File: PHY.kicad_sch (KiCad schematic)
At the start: 52 parts, among them U1 LAN83C185-JT, Y1 25 MHz

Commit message: did a lot more routing, phy nearly done
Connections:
- net MAG-RXn renamed MAG-RXN
- net MAG-RXp renamed MAG-RXP
- net MAG-TXn renamed MAG-TXN
- net MAG-TXp renamed MAG-TXP
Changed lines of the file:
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@@
     )
   )
-  (global_label "MAG-TXp" (shape input) (at 190.5 82.55 0) (fields_autoplaced)
+  (global_label "MAG-TXP" (shape input) (at 190.5 82.55 0) (fields_autoplaced)
     (effects (font (size 1.27 1.27)) (justify left))
-    (property "Intersheet References" "${INTERSHEET_REFS}" (id 0) (at 201.6217 82.6294 0)
+    (property "Intersheet References" "${INTERSHEET_REFS}" (id 0) (at 201.7426 82.4706 0)
       (effects (font (size 1.27 1.27)) (justify left) hide)
     )
@@
     )
   )
-  (global_label "MAG-TXn" (shape input) (at 190.5 85.09 0) (fields_autoplaced)
+  (global_label "MAG-TXN" (shape input) (at 190.5 85.09 0) (fields_autoplaced)
     (effects (font (size 1.27 1.27)) (justify left))
-    (property "Intersheet References" "${INTERSHEET_REFS}" (id 0) (at 201.6217 85.0106 0)
+    (property "Intersheet References" "${INTERSHEET_REFS}" (id 0) (at 201.8031 85.0106 0)
       (effects (font (size 1.27 1.27)) (justify left) hide)
     )
@@
     )
   )
-  (global_label "MAG-RXn" (shape input) (at 190.5 74.93 0) (fields_autoplaced)
+  (global_label "MAG-RXN" (shape input) (at 190.5 74.93 0) (fields_autoplaced)
     (effects (font (size 1.27 1.27)) (justify left))
-    (property "Intersheet References" "${INTERSHEET_REFS}" (id 0) (at 201.9241 74.8506 0)
+    (property "Intersheet References" "${INTERSHEET_REFS}" (id 0) (at 202.1055 74.8506 0)
       (effects (font (size 1.27 1.27)) (justify left) hide)
     )
@@
     )
   )
-  (global_label "MAG-RXp" (shape input) (at 190.5 72.39 0) (fields_autoplaced)
+  (global_label "MAG-RXP" (shape input) (at 190.5 72.39 0) (fields_autoplaced)
     (effects (font (size 1.27 1.27)) (justify left))
-    (property "Intersheet References" "${INTERSHEET_REFS}" (id 0) (at 201.9241 72.3106 0)
+    (property "Intersheet References" "${INTERSHEET_REFS}" (id 0) (at 202.045 72.3106 0)
       (effects (font (size 1.27 1.27)) (justify left) hide)
     )

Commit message: Update sourcing URLs
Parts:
- D1, D5: Source https://onecall.farnell.com/dialight/599-0240-007f/led-yellow-126mcd-590nm-1206/dp/3548450?st=yellow -> https://onecall.farnell.com/dialight/599-0240-007f/led-yellow-126mcd-590nm-1206/dp/3548450
- FB1, FB2, FB3: Source https://uk.farnell.com/bourns/mh3261-601y/ferrite-bead-0-1o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 -> https://onecall.farnell.com/bourns/mh3261-601y/ferrite-bead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
- U1: Source https://uk.rs-online.com/web/p/physical-layer-transceivers/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 -> https://onecall.farnell.com/microchip/lan83c185-jt/transcei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
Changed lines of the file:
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@@
       (effects (font (size 1.27 1.27)) hide)
     )
-    (property "Source" "https://uk.farnell.com/bourns/mh3261-601y/ferrite-bead-0-1ohm-2a-1206/dp/27870" (id 4) (at 115.57 172.72 0)
+    (property "Source" "https://onecall.farnell.com/bourns/mh3261-601y/ferrite-bead-0-1ohm-2a-1206/dp/2787025" (id 4) (at 115.57 172.72 0)
       (effects (font (size 1.27 1.27)) hide)
     )
@@
       (effects (font (size 1.27 1.27)) hide)
     )
-    (property "Source" "https://onecall.farnell.com/dialight/599-0240-007f/led-yellow-126mcd-590nm-1206/dp/3548450?st=yellow" (id 4) (at 255.27 31.75 0)
+    (property "Source" "https://onecall.farnell.com/dialight/599-0240-007f/led-yellow-126mcd-590nm-1206/dp/3548450" (id 4) (at 255.27 31.75 0)
       (effects (font (size 1.27 1.27)) hide)
     )
@@
       (effects (font (size 1.27 1.27)) hide)
     )
-    (property "Source" "https://uk.farnell.com/bourns/mh3261-601y/ferrite-bead-0-1ohm-2a-1206/dp/27870" (id 4) (at 27.94 172.72 0)
+    (property "Source" "https://onecall.farnell.com/bourns/mh3261-601y/ferrite-bead-0-1ohm-2a-1206/dp/2787025" (id 4) (at 27.94 172.72 0)
       (effects (font (size 1.27 1.27)) hide)
     )
@@
       (effects (font (size 1.27 1.27)) hide)
     )
-    (property "Source" "https://uk.farnell.com/bourns/mh3261-601y/ferrite-bead-0-1ohm-2a-1206/dp/27870" (id 4) (at 80.01 172.72 0)
+    (property "Source" "https://onecall.farnell.com/bourns/mh3261-601y/ferrite-bead-0-1ohm-2a-1206/dp/2787025" (id 4) (at 80.01 172.72 0)
       (effects (font (size 1.27 1.27)) hide)
     )
@@
       (effects (font (size 1.524 1.524)) hide)
     )
-    (property "Source" "https://uk.rs-online.com/web/p/physical-layer-transceivers/6726806" (id 4) (at 93.98 49.53 0)
+    (property "Source" "https://onecall.farnell.com/microchip/lan83c185-jt/transceiver-phy-10-100-64tqfp/dp/1711344" (id 4) (at 93.98 49.53 0)
       (effects (font (size 1.27 1.27)) hide)
     )
@@
       (effects (font (size 1.27 1.27)) hide)
     )
-    (property "Source" "https://onecall.farnell.com/dialight/599-0240-007f/led-yellow-126mcd-590nm-1206/dp/3548450?st=yellow" (id 4) (at 219.71 31.75 0)
-      (effects (font (size 1.27 1.27)) hide)
-    )
+    (property "Source" "https://onecall.farnell.com/dialight/599-0240-007f/led-yellow-126mcd-590nm-1206/dp/3548450" (id 4) (at 219.71 31.75 0)
+      (effects (font (size 1.27 1.27)) hide)
+    )

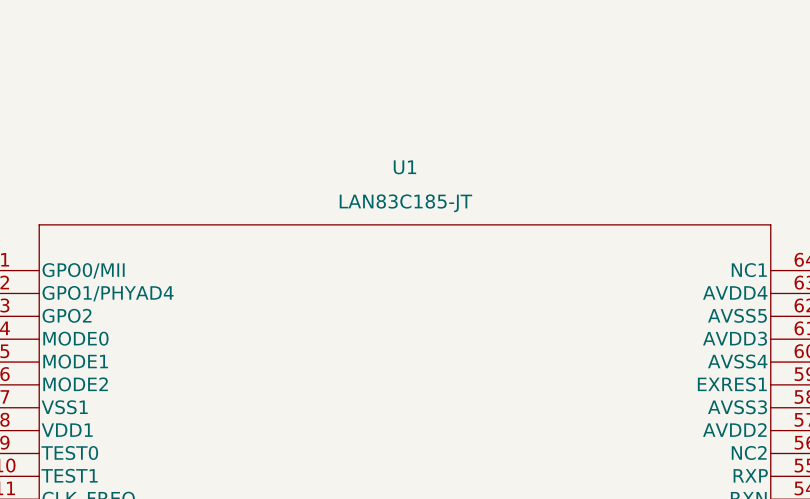
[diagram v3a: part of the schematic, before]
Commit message: Change QFP footprint to 0.25mm gap
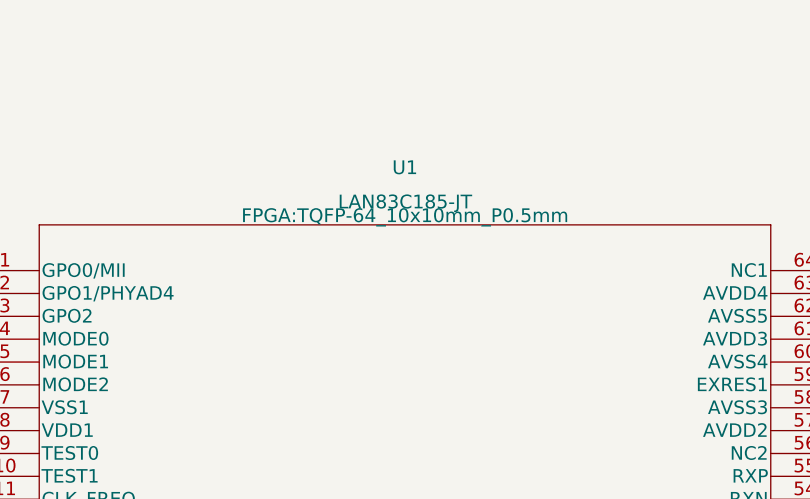
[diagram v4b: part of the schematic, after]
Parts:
- U1: footprint Package_QFP:TQFP-64_10x10mm_P0.5mm -> FPGA:TQFP-64_10x10mm_P0.5mm
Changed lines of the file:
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@@
       (effects (font (size 1.524 1.524)))
     )
-    (property "Footprint" "Package_QFP:TQFP-64_10x10mm_P0.5mm" (id 2) (at 142.24 43.434 0)
-      (effects (font (size 1.524 1.524)) hide)
+    (property "Footprint" "FPGA:TQFP-64_10x10mm_P0.5mm" (id 2) (at 142.24 43.434 0)
+      (effects (font (size 1.524 1.524)))
     )
     (property "Datasheet" "https://docs.rs-online.com/1038/0900766b80d9640a.pdf" (id 3) (at 93.98 49.53 0)

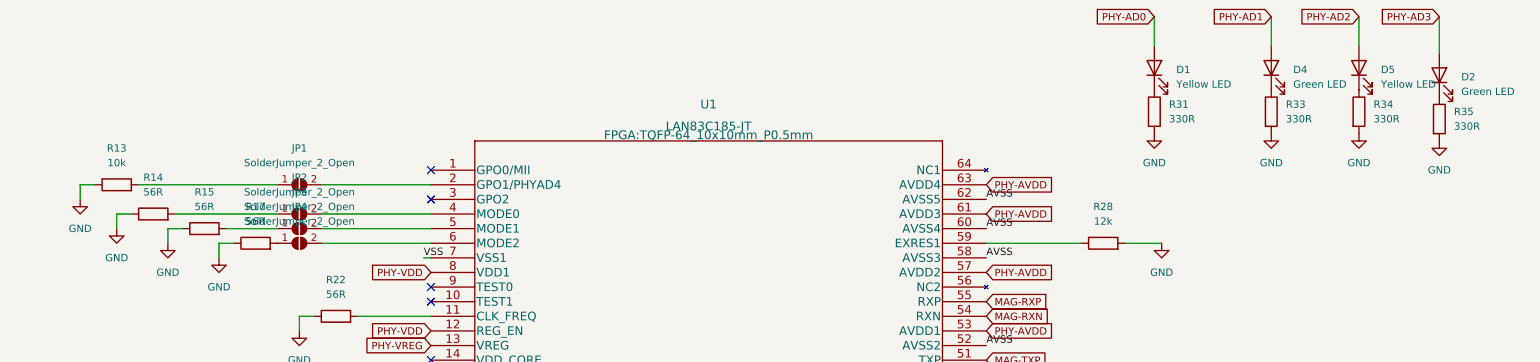
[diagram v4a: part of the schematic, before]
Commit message: made 2nd rev changes to ethernet side
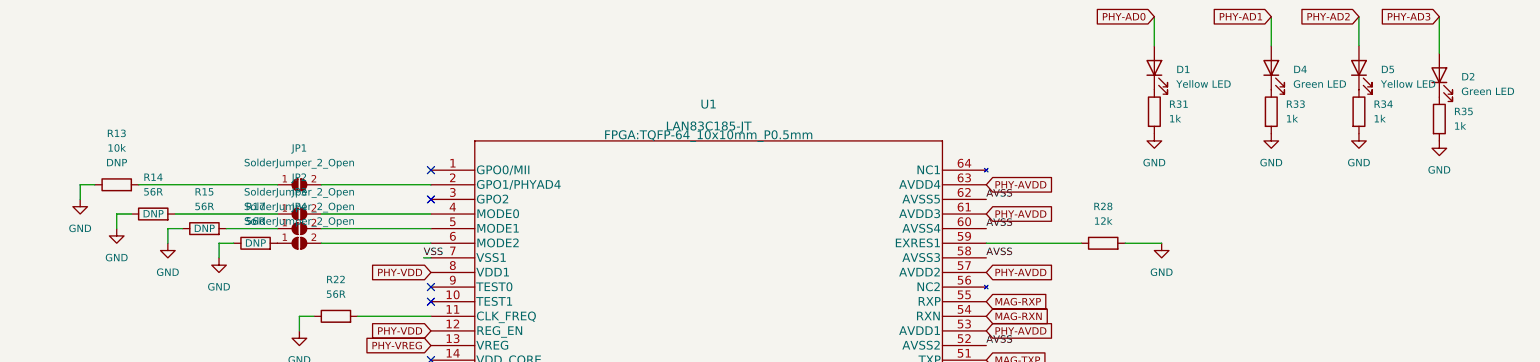
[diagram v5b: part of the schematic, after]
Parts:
- R13, R14, R15, R17: DNP (none) -> DNP
- R31, R33, R34, R35: value 330R -> 1k
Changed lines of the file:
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@@
       (effects (font (size 1.27 1.27)) hide)
     )
+    (property "DNP" "DNP" (id 5) (at 63.5 62.23 90))
     (pin "1")
     (pin "2")
@@
       (effects (font (size 1.27 1.27)) hide)
     )
+    (property "DNP" "DNP" (id 5) (at 54.61 59.69 90))
     (pin "1")
     (pin "2")
@@
       (effects (font (size 1.27 1.27)) (justify left))
     )
-    (property "Value" "330R" (id 1) (at 222.25 40.6399 0)
+    (property "Value" "1k" (id 1) (at 222.25 40.6399 0)
       (effects (font (size 1.27 1.27)) (justify left))
     )
@@
       (effects (font (size 1.27 1.27)) (justify left))
     )
-    (property "Value" "330R" (id 1) (at 257.81 40.6399 0)
+    (property "Value" "1k" (id 1) (at 257.81 40.6399 0)
       (effects (font (size 1.27 1.27)) (justify left))
     )
@@
       (effects (font (size 1.27 1.27)) hide)
     )
+    (property "DNP" "DNP" (id 5) (at 45.72 57.15 90))
     (pin "1")
     (pin "2")
@@
   (symbol (lib_id "Device:R") (at 39.37 52.07 90) (unit 1)
     (in_bom yes) (on_board yes) (fields_autoplaced)
-    (property "Reference" "R13" (id 0) (at 39.37 45.72 90))
-    (property "Value" "10k" (id 1) (at 39.37 48.26 90))
+    (property "Reference" "R13" (id 0) (at 39.37 43.18 90))
+    (property "Value" "10k" (id 1) (at 39.37 45.72 90))
     (property "Footprint" "Resistor_SMD:R_0805_2012Metric_Pad1.20x1.40mm_HandSolder" (id 2) (at 39.37 53.848 90)
       (effects (font (size 1.27 1.27)) hide)
@@
       (effects (font (size 1.27 1.27)) hide)
     )
+    (property "DNP" "DNP" (id 5) (at 39.37 48.26 90))
     (pin "1")
     (pin "2")
@@
       (effects (font (size 1.27 1.27)) (justify left))
     )
-    (property "Value" "330R" (id 1) (at 271.78 41.9099 0)
+    (property "Value" "1k" (id 1) (at 271.78 41.9099 0)
       (effects (font (size 1.27 1.27)) (justify left))
     )
@@
       (effects (font (size 1.27 1.27)) (justify left))
     )
-    (property "Value" "330R" (id 1) (at 242.57 40.6399 0)
-      (effects (font (size 1.27 1.27)) (justify left))
-    )
+    (property "Value" "1k" (id 1) (at 242.57 40.6399 0)
+      (effects (font (size 1.27 1.27)) (justify left))
+    )
